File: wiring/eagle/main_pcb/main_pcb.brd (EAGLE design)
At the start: 100.1 x 79.8 mm, 19 parts

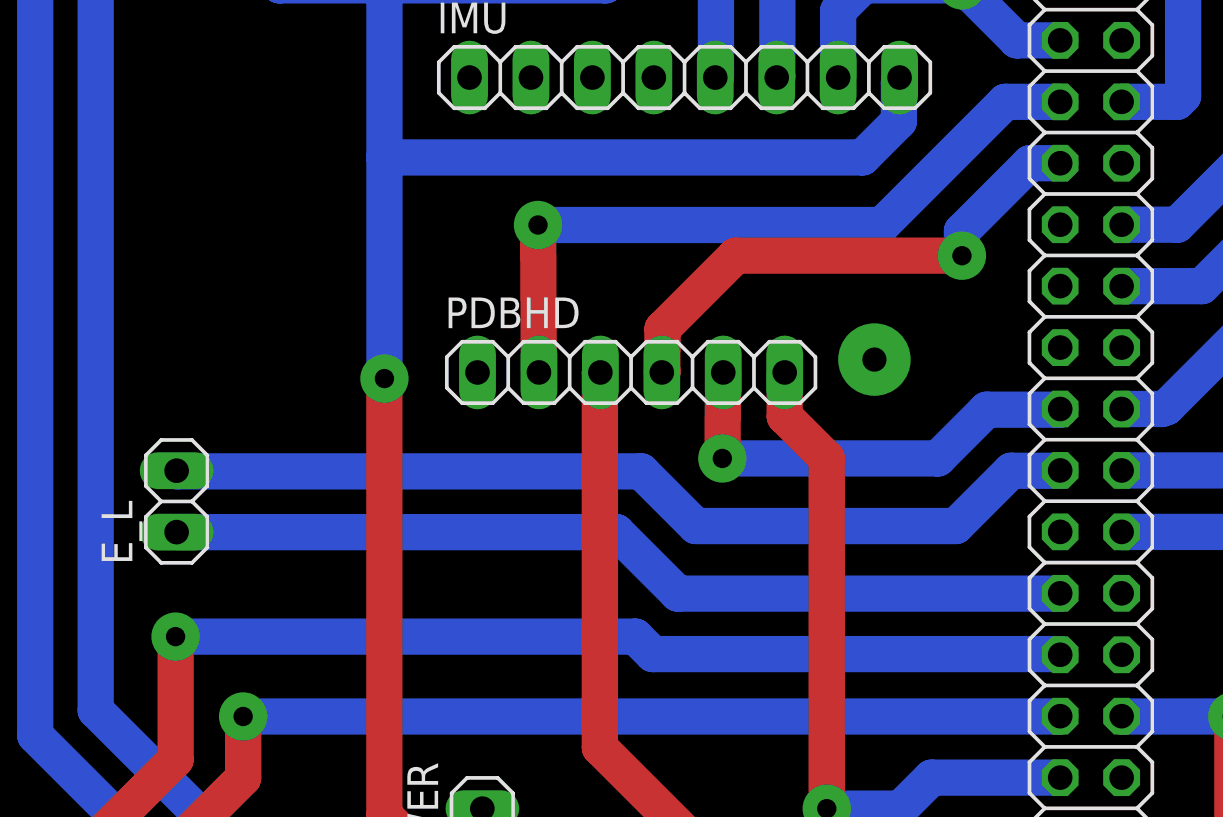
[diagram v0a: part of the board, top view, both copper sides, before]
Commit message: Make changes to PCB to avoid using pin 27
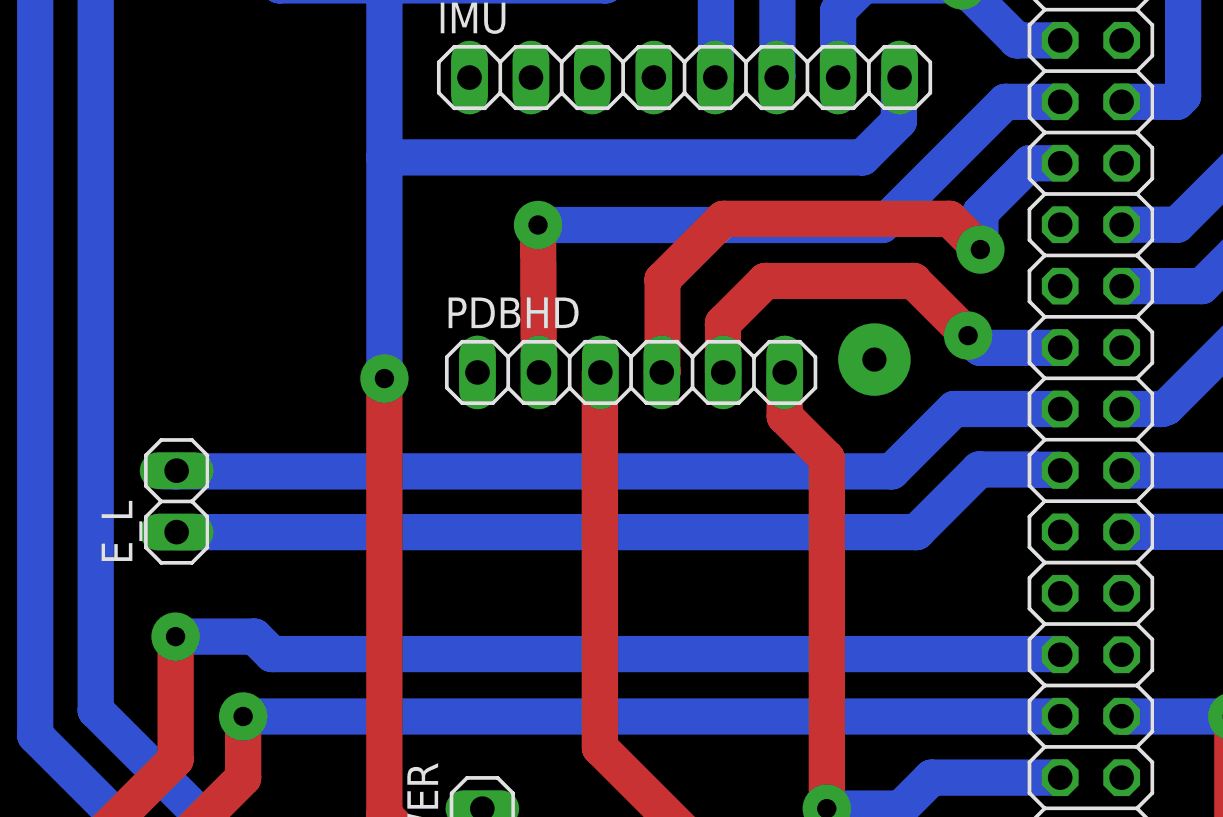
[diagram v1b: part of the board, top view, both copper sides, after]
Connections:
- removed net EL_A: E_L.2, PIHD.23
- removed net EL_B: E_L.1, PIHD.27
- new net N$1: E_L.2, PIHD.21
- new net N$2: E_L.1, PIHD.23
- net RDIR: now also PIHD.19; no longer PIHD.21
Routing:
- net EL_A: track 38.4 -> 0.00 mm
- net N$1: track 0.00 -> 38.2 mm
- net N$2: track 0.00 -> 37.6 mm
- net EL_B: track 37.6 -> 0.00 mm
- net SLP: track 21.7 -> 24.2 mm
- net RDIR: track 18.4 -> 17.9 mm
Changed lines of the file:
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@@
 <layers>
 <layer number="1" name="Top" color="4" fill="1" visible="yes" active="yes"/>
-<layer number="16" name="Bottom" color="1" fill="1" visible="no" active="yes"/>
+<layer number="16" name="Bottom" color="1" fill="1" visible="yes" active="yes"/>
 <layer number="17" name="Pads" color="2" fill="1" visible="yes" active="yes"/>
 <layer number="18" name="Vias" color="2" fill="1" visible="yes" active="yes"/>
@@
 <contactref element="PDBHD" pad="4"/>
 <contactref element="PIHD" pad="13"/>
-<wire x1="49.088" y1="33.04450625" x2="49.088" y2="31.27" width="1.5" layer="1"/>
+<wire x1="49.088" y1="35.07650625" x2="49.088" y2="31.27" width="1.5" layer="1"/>
 <wire x1="49.088" y1="31.27" x2="49.06" y2="31.242" width="1.5" layer="1"/>
-<wire x1="61.468" y1="36.068" x2="52.11149375" y2="36.068" width="1.5" layer="1"/>
-<wire x1="52.11149375" y1="36.068" x2="49.088" y2="33.04450625" width="1.5" layer="1"/>
-<via x="61.468" y="36.068" extent="1-16" drill="0.8" diameter="2"/>
-<wire x1="64.274" y1="39.89" x2="61.468" y2="37.084" width="1.5" layer="16"/>
-<wire x1="61.468" y1="37.084" x2="61.468" y2="36.068" width="1.5" layer="16"/>
+<wire x1="62.23" y1="36.322" x2="60.96" y2="37.592" width="1.5" layer="1"/>
+<wire x1="60.96" y1="37.592" x2="51.60349375" y2="37.592" width="1.5" layer="1"/>
+<wire x1="51.60349375" y1="37.592" x2="49.088" y2="35.07650625" width="1.5" layer="1"/>
+<via x="62.23" y="36.322" extent="1-16" drill="0.8" diameter="2"/>
+<wire x1="64.274" y1="39.89" x2="62.23" y2="37.846" width="1.5" layer="16"/>
+<wire x1="62.23" y1="37.846" x2="62.23" y2="36.322" width="1.5" layer="16"/>
 <wire x1="65.53" y1="39.89" x2="64.274" y2="39.89" width="1.5" layer="16"/>
 </signal>
 <signal name="RDIR">
 <contactref element="PDBHD" pad="5"/>
-<via x="51.562" y="27.686" extent="1-16" drill="0.8" diameter="2"/>
-<wire x1="51.562" y1="27.686" x2="51.6" y2="31.242" width="1.5" layer="1"/>
-<contactref element="PIHD" pad="21"/>
-<wire x1="65.502" y1="29.702" x2="65.53" y2="29.73" width="1.5" layer="16"/>
-<wire x1="60.4724625" y1="27.686" x2="62.4884625" y2="29.702" width="1.5" layer="16"/>
-<wire x1="62.4884625" y1="29.702" x2="65.502" y2="29.702" width="1.5" layer="16"/>
-<wire x1="51.562" y1="27.686" x2="60.4724625" y2="27.686" width="1.5" layer="16"/>
+<contactref element="PIHD" pad="19"/>
+<wire x1="51.6" y1="31.242" x2="51.588" y2="31.254" width="1.5" layer="1"/>
+<wire x1="51.588" y1="31.254" x2="51.588" y2="33.274" width="1.5" layer="1"/>
+<wire x1="51.588" y1="33.274" x2="53.338" y2="35.024" width="1.5" layer="1"/>
+<wire x1="53.338" y1="35.024" x2="59.464" y2="35.024" width="1.5" layer="1"/>
+<wire x1="59.464" y1="35.024" x2="61.722" y2="32.766" width="1.5" layer="1"/>
+<via x="61.722" y="32.766" extent="1-16" drill="0.8" diameter="2"/>
+<wire x1="65.518" y1="32.258" x2="62.23" y2="32.258" width="1.5" layer="16"/>
+<wire x1="62.23" y1="32.258" x2="61.722" y2="32.766" width="1.5" layer="16"/>
+<wire x1="65.53" y1="32.27" x2="65.518" y2="32.258" width="1.5" layer="16"/>
 </signal>
 <signal name="LPWM">
@@
 <wire x1="21.844" y1="9.398" x2="18.034" y2="5.588" width="1.5" layer="16"/>
 <wire x1="18.034" y1="5.588" x2="15.24" y2="5.588" width="1.5" layer="16"/>
-<wire x1="28.956" y1="20.32" x2="47.9678375" y2="20.32" width="1.5" layer="16"/>
-<wire x1="47.9678375" y1="20.32" x2="48.6898375" y2="19.598" width="1.5" layer="16"/>
-<wire x1="48.6898375" y1="19.598" x2="65.502" y2="19.598" width="1.5" layer="16"/>
+<wire x1="28.956" y1="20.32" x2="32.2198375" y2="20.32" width="1.5" layer="16"/>
+<wire x1="32.2198375" y1="20.32" x2="32.9418375" y2="19.598" width="1.5" layer="16"/>
+<wire x1="32.9418375" y1="19.598" x2="65.502" y2="19.598" width="1.5" layer="16"/>
 <wire x1="65.502" y1="19.598" x2="65.53" y2="19.57" width="1.5" layer="16"/>
 <wire x1="28.956" y1="15.24" x2="28.956" y2="20.32" width="1.5" layer="1"/>
@@
 <wire x1="70.37" y1="37.35" x2="73.152" y2="40.132" width="1.5" layer="16"/>
 </signal>
-<signal name="EL_A">
-<contactref element="E_L" pad="2"/>
-<contactref element="PIHD" pad="23"/>
-<wire x1="50.4669125" y1="24.892" x2="61.214" y2="24.892" width="1.5" layer="16"/>
-<wire x1="61.214" y1="24.892" x2="63.5" y2="27.178" width="1.5" layer="16"/>
-<wire x1="63.5" y1="27.178" x2="65.518" y2="27.178" width="1.5" layer="16"/>
-<wire x1="65.518" y1="27.178" x2="65.53" y2="27.19" width="1.5" layer="16"/>
-<wire x1="29" y1="27.18" x2="29.028" y2="27.152" width="1.5" layer="16"/>
-<wire x1="29.028" y1="27.152" x2="48.2069125" y2="27.152" width="1.5" layer="16"/>
-<wire x1="48.2069125" y1="27.152" x2="50.4669125" y2="24.892" width="1.5" layer="16"/>
-</signal>
-<signal name="EL_B">
-<contactref element="E_L" pad="1"/>
-<contactref element="PIHD" pad="27"/>
-<wire x1="65.518" y1="22.098" x2="65.53" y2="22.11" width="1.5" layer="16"/>
-<wire x1="65.518" y1="22.098" x2="49.725375" y2="22.098" width="1.5" layer="16"/>
-<wire x1="47.183375" y1="24.64" x2="29" y2="24.64" width="1.5" layer="16"/>
-<wire x1="49.725375" y1="22.098" x2="47.183375" y2="24.64" width="1.5" layer="16"/>
-</signal>
 <signal name="ER_A">
 <contactref element="E_R" pad="1"/>
@@
 <via x="57.85" y="31.774" extent="1-16" drill="1" diameter="3"/>
 </signal>
+<signal name="N$1">
+<contactref element="E_L" pad="2"/>
+<contactref element="PIHD" pad="21"/>
+<wire x1="65.53" y1="29.73" x2="61.1437375" y2="29.73" width="1.5" layer="16"/>
+<wire x1="61.1437375" y1="29.73" x2="58.5657375" y2="27.152" width="1.5" layer="16"/>
+<wire x1="58.5657375" y1="27.152" x2="28.972" y2="27.152" width="1.5" layer="16"/>
+<wire x1="28.448" y1="27.152" x2="28.972" y2="27.152" width="1.5" layer="16"/>
+<wire x1="28.972" y1="27.152" x2="29" y2="27.18" width="1.5" layer="16"/>
+</signal>
+<signal name="N$2">
+<contactref element="E_L" pad="1"/>
+<contactref element="PIHD" pad="23"/>
+<wire x1="29" y1="24.64" x2="59.589275" y2="24.64" width="1.5" layer="16"/>
+<wire x1="59.589275" y1="24.64" x2="62.179275" y2="27.23" width="1.5" layer="16"/>
+<wire x1="62.179275" y1="27.23" x2="64.47749375" y2="27.23" width="1.5" layer="16"/>
+<wire x1="64.47749375" y1="27.23" x2="64.48949375" y2="27.218" width="1.5" layer="16"/>
+<wire x1="64.48949375" y1="27.218" x2="65.502" y2="27.218" width="1.5" layer="16"/>
+<wire x1="65.502" y1="27.218" x2="65.53" y2="27.19" width="1.5" layer="16"/>
+</signal>
 </signals>
